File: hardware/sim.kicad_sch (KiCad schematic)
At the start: 11 parts, among them J12 PRPC006SAAN-RC, J13 G85D1160022HHR

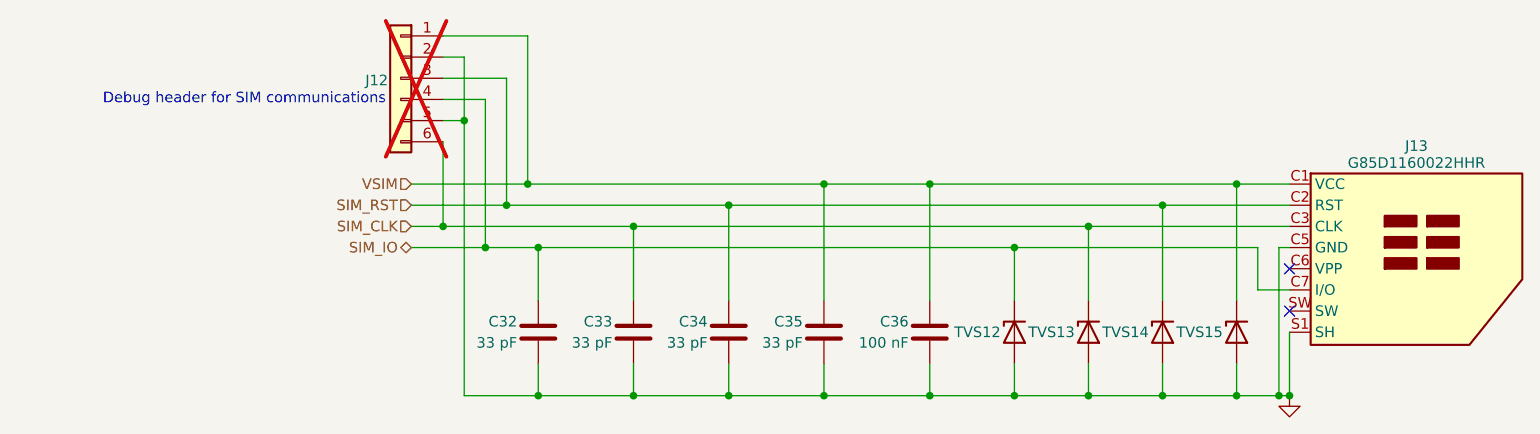
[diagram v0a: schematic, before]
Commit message: HW: Add battery protection
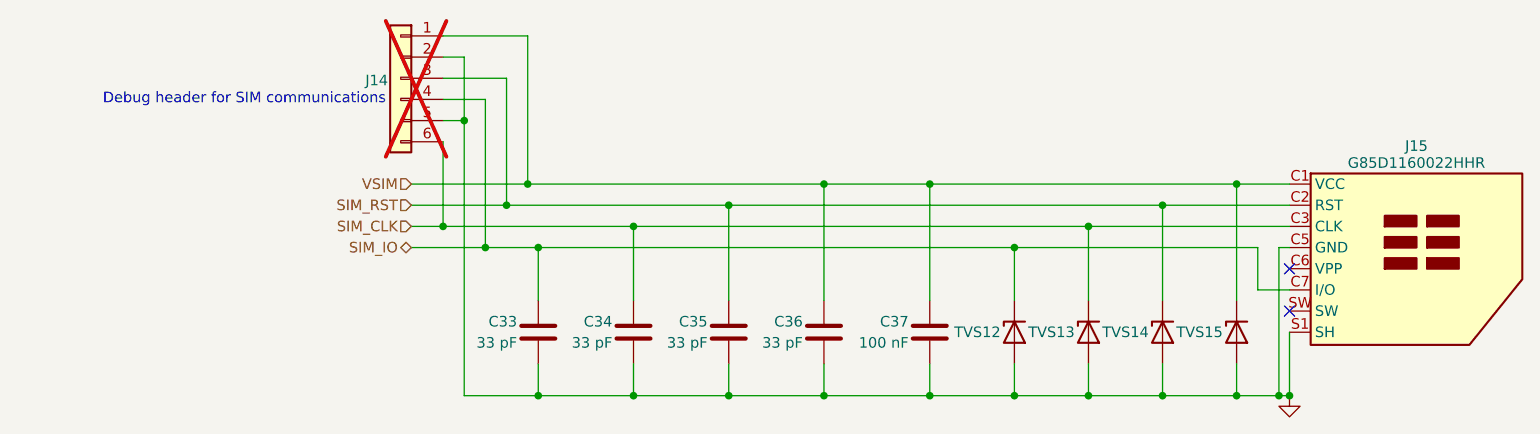
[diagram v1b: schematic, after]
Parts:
- renumbered C32 to C33, C33 to C34, C34 to C35, C35 to C36, C36 to C37, J12 to J14, J13 to J15
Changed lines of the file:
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@@
 		(on_board yes)
 		(dnp no)
-		(property "Reference" "C36"
+		(property "Reference" "C37"
 			(at 143.51 135.89 0)
 			(effects
@@
 			(project "iida_devkit"
 				(path "/b12a6e25-97fb-4aba-bc96-af8db389bb9a/33580d9f-a609-4568-baaf-9a29cf2dabcd"
-					(reference "C36")
+					(reference "C37")
 					(unit 1)
 				)
@@
 		(on_board yes)
 		(dnp yes)
-		(property "Reference" "J12"
+		(property "Reference" "J14"
 			(at 81.026 106.934 0)
 			(effects
@@
 			(project "iida_devkit"
 				(path "/b12a6e25-97fb-4aba-bc96-af8db389bb9a/33580d9f-a609-4568-baaf-9a29cf2dabcd"
-					(reference "J12")
+					(reference "J14")
 					(unit 1)
 				)
@@
 		(on_board yes)
 		(dnp no)
-		(property "Reference" "C33"
+		(property "Reference" "C34"
 			(at 107.95 135.89 0)
 			(effects
@@
 			(project "iida_devkit"
 				(path "/b12a6e25-97fb-4aba-bc96-af8db389bb9a/33580d9f-a609-4568-baaf-9a29cf2dabcd"
-					(reference "C33")
+					(reference "C34")
 					(unit 1)
 				)
@@
 		(on_board yes)
 		(dnp no)
-		(property "Reference" "C32"
+		(property "Reference" "C33"
 			(at 96.52 135.89 0)
 			(effects
@@
 			(project "iida_devkit"
 				(path "/b12a6e25-97fb-4aba-bc96-af8db389bb9a/33580d9f-a609-4568-baaf-9a29cf2dabcd"
-					(reference "C32")
+					(reference "C33")
 					(unit 1)
 				)
@@
 		(on_board yes)
 		(dnp no)
-		(property "Reference" "C34"
+		(property "Reference" "C35"
 			(at 119.38 135.89 0)
 			(effects
@@
 			(project "iida_devkit"
 				(path "/b12a6e25-97fb-4aba-bc96-af8db389bb9a/33580d9f-a609-4568-baaf-9a29cf2dabcd"
-					(reference "C34")
+					(reference "C35")
 					(unit 1)
 				)
@@
 		(on_board yes)
 		(dnp no)
-		(property "Reference" "J13"
+		(property "Reference" "J15"
 			(at 204.47 114.808 0)
 			(effects
@@
 			(project "iida_devkit"
 				(path "/b12a6e25-97fb-4aba-bc96-af8db389bb9a/33580d9f-a609-4568-baaf-9a29cf2dabcd"
-					(reference "J13")
+					(reference "J15")
 					(unit 1)
 				)
@@
 		(dnp no)
 		(fields_autoplaced yes)
-		(property "Reference" "#PWR056"
+		(property "Reference" "#PWR058"
 			(at 189.23 151.13 0)
 			(effects
@@
 			(project "iida_devkit"
 				(path "/b12a6e25-97fb-4aba-bc96-af8db389bb9a/33580d9f-a609-4568-baaf-9a29cf2dabcd"
-					(reference "#PWR056")
+					(reference "#PWR058")
 					(unit 1)
 				)
@@
 		(on_board yes)
 		(dnp no)
-		(property "Reference" "C35"
+		(property "Reference" "C36"
 			(at 130.81 135.89 0)
 			(effects
@@
 			(project "iida_devkit"
 				(path "/b12a6e25-97fb-4aba-bc96-af8db389bb9a/33580d9f-a609-4568-baaf-9a29cf2dabcd"
-					(reference "C35")
+					(reference "C36")
 					(unit 1)
 				)

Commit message: HW: Replace 0402 with 0603 or bigger
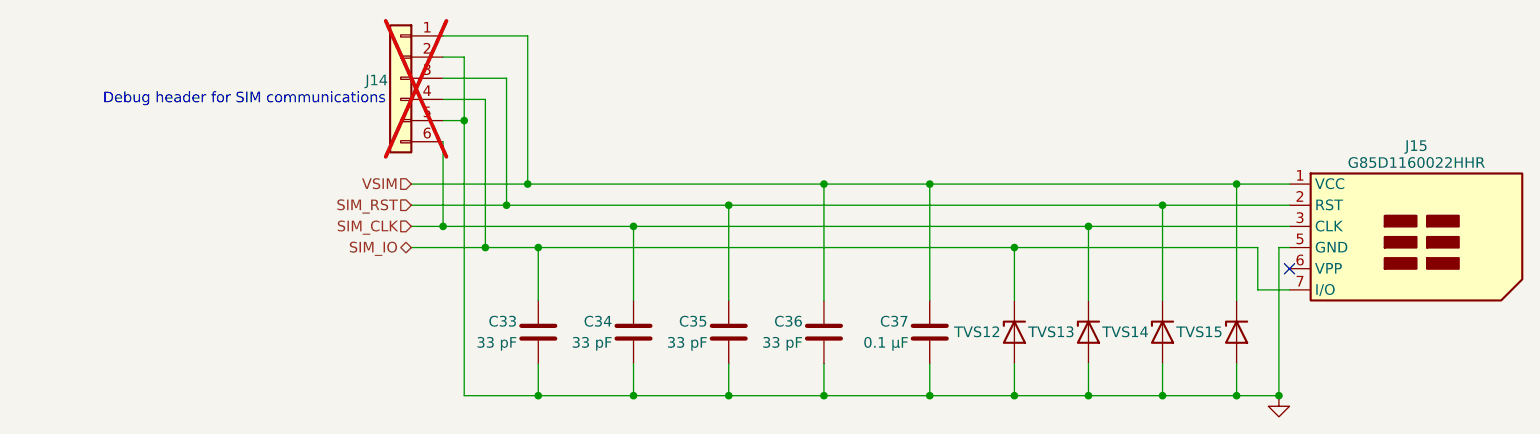
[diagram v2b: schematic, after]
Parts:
- C33, C34, C35, C36: footprint Capacitor_SMD:C_0402_1005Metric_Pad0.74x0.62mm_HandSolder -> Capacitor_SMD:C_0603_1608Metric_Pad1.08x0.95mm_HandSolder; Digi-Key Part Number 732-7472-1-ND -> 732-7749-1-ND; Manufacturer Part Number 885012005058 -> 885012006005
- C37: value 100 nF -> 0.1 µF; footprint Capacitor_SMD:C_0402_1005Metric_Pad0.74x0.62mm_HandSolder -> Capacitor_SMD:C_0603_1608Metric_Pad1.08x0.95mm_HandSolder; Digi-Key Part Number 732-7513-1-ND -> 732-7989-1-ND; Manufacturer Part Number 885012205018 -> 885012206071
- TVS12, TVS13, TVS14, TVS15: value PE1605M1Q_R1_00001 -> CPDUC5V0USP-HF; footprint Diode_SMD:D_0402_1005Metric_Pad0.77x0.64mm_HandSolder -> Diode_SMD:D_0603_1608Metric_Pad1.05x0.95mm_HandSolder; Digi-Key Part Number 3757-PE1605M1Q_R1_00001CT-ND -> 641-1765-1-ND; Manufacturer Panjit International Inc. -> Comchip Technology; Manufacturer Part Number PE1605M1Q_R1_00001 -> CPDUC5V0USP-HF
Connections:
- net GND: now also J15.5 (GND); no longer J15.C5 (GND), J15.S1 (SH), J15.S2 (SH), J15.S3 (SH)
- net SIM_CLK: now also J15.3 (CLK); no longer J15.C3 (CLK)
- net SIM_IO: now also J15.7 (I/O); no longer J15.C7 (I/O)
- net SIM_RST: now also J15.2 (RST); no longer J15.C2 (RST)
- net VSIM: now also J15.1 (VCC); no longer J15.C1 (VCC)
- no-connect marks 2 -> 1
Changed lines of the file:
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@@
 	)
 	(junction
-		(at 189.23 144.78)
-		(diameter 0)
-		(color 0 0 0 0)
-	)
-	(junction
 		(at 110.49 124.46)
 		(diameter 0)
@@
 		(at 189.23 129.54)
 	)
-	(no_connect
-		(at 189.23 134.62)
-	)
 	(wire
 		(pts
@@
 	(wire
 		(pts
-			(xy 189.23 144.78) (xy 187.96 144.78)
-		)
-		(stroke
-			(width 0)
-			(type default)
-		)
-	)
-	(wire
-		(pts
 			(xy 133.35 140.97) (xy 133.35 144.78)
 		)
@@
 	(wire
 		(pts
-			(xy 189.23 137.16) (xy 189.23 144.78)
-		)
-		(stroke
-			(width 0)
-			(type default)
-		)
-	)
-	(wire
-		(pts
 			(xy 156.21 144.78) (xy 165.1 144.78)
 		)
@@
 			)
 		)
-		(property "Value" "100 nF"
+		(property "Value" "0.1 µF"
 			(at 143.51 138.43 0)
 			(effects
@@
 			)
 		)
-		(property "Footprint" "Capacitor_SMD:C_0402_1005Metric_Pad0.74x0.62mm_HandSolder"
+		(property "Footprint" "Capacitor_SMD:C_0603_1608Metric_Pad1.08x0.95mm_HandSolder"
 			(at 145.0848 140.97 0)
 			(effects
@@
 			)
 		)
-		(property "Manufacturer Part Number" "885012205018"
+		(property "Manufacturer Part Number" "885012206071"
 			(at 146.05 137.16 0)
 			(effects
@@
 			)
 		)
-		(property "Digi-Key Part Number" "732-7513-1-ND"
+		(property "Digi-Key Part Number" "732-7989-1-ND"
 			(at 146.05 137.16 0)
 			(effects
@@
 			)
 		)
-		(property "Value" "PE1605M1Q_R1_00001"
+		(property "Value" "CPDUC5V0USP-HF"
 			(at 154.94 138.43 90)
 			(effects
@@
 			)
 		)
-		(property "Footprint" "Diode_SMD:D_0402_1005Metric_Pad0.77x0.64mm_HandSolder"
+		(property "Footprint" "Diode_SMD:D_0603_1608Metric_Pad1.05x0.95mm_HandSolder"
 			(at 165.1 137.16 0)
 			(effects
@@
 			)
 		)
-		(property "Digi-Key Part Number" "3757-PE1605M1Q_R1_00001CT-ND"
+		(property "Digi-Key Part Number" "641-1765-1-ND"
 			(at 165.1 137.16 0)
 			(effects
@@
 			)
 		)
-		(property "Manufacturer" "Panjit International Inc."
+		(property "Manufacturer" "Comchip Technology"
 			(at 165.1 137.16 0)
 			(effects
@@
 			)
 		)
-		(property "Manufacturer Part Number" "PE1605M1Q_R1_00001"
+		(property "Manufacturer Part Number" "CPDUC5V0USP-HF"
 			(at 165.1 137.16 0)
 			(effects
@@
 			)
 		)
-		(property "Footprint" "Capacitor_SMD:C_0402_1005Metric_Pad0.74x0.62mm_HandSolder"
+		(property "Footprint" "Capacitor_SMD:C_0603_1608Metric_Pad1.08x0.95mm_HandSolder"
 			(at 111.4552 140.97 0)
 			(effects
@@
 			)
 		)
-		(property "Digi-Key Part Number" "732-7472-1-ND"
+		(property "Digi-Key Part Number" "732-7749-1-ND"
 			(at 110.49 137.16 0)
 			(effects
@@
 			)
 		)
-		(property "Manufacturer Part Number" "885012005058"
+		(property "Manufacturer Part Number" "885012006005"
 			(at 110.49 137.16 0)
 			(effects
@@
 			)
 		)
-		(property "Footprint" "Capacitor_SMD:C_0402_1005Metric_Pad0.74x0.62mm_HandSolder"
+		(property "Footprint" "Capacitor_SMD:C_0603_1608Metric_Pad1.08x0.95mm_HandSolder"
 			(at 100.0252 140.97 0)
 			(effects
@@
 			)
 		)
-		(property "Digi-Key Part Number" "732-7472-1-ND"
+		(property "Digi-Key Part Number" "732-7749-1-ND"
 			(at 99.06 137.16 0)
 			(effects
@@
 			)
 		)
-		(property "Manufacturer Part Number" "885012005058"
+		(property "Manufacturer Part Number" "885012006005"
 			(at 99.06 137.16 0)
 			(effects
@@
 			)
 		)
-		(property "Value" "PE1605M1Q_R1_00001"
+		(property "Value" "CPDUC5V0USP-HF"
 			(at 172.72 138.43 90)
 			(effects
@@
 			)
 		)
-		(property "Footprint" "Diode_SMD:D_0402_1005Metric_Pad0.77x0.64mm_HandSolder"
+		(property "Footprint" "Diode_SMD:D_0603_1608Metric_Pad1.05x0.95mm_HandSolder"
 			(at 182.88 137.16 0)
 			(effects
@@
 			)
 		)
-		(property "Digi-Key Part Number" "3757-PE1605M1Q_R1_00001CT-ND"
+		(property "Digi-Key Part Number" "641-1765-1-ND"
 			(at 182.88 137.16 0)
 			(effects
@@
 			)
 		)
-		(property "Manufacturer" "Panjit International Inc."
+		(property "Manufacturer" "Comchip Technology"
 			(at 182.88 137.16 0)
 			(effects
@@
 			)
 		)
-		(property "Manufacturer Part Number" "PE1605M1Q_R1_00001"
+		(property "Manufacturer Part Number" "CPDUC5V0USP-HF"
 			(at 182.88 137.16 0)
 			(effects
@@
 			)
 		)
-		(property "Value" "PE1605M1Q_R1_00001"
+		(property "Value" "CPDUC5V0USP-HF"
 			(at 146.05 138.43 90)
 			(effects
@@
 			)
 		)
-		(property "Footprint" "Diode_SMD:D_0402_1005Metric_Pad0.77x0.64mm_HandSolder"
+		(property "Footprint" "Diode_SMD:D_0603_1608Metric_Pad1.05x0.95mm_HandSolder"
 			(at 156.21 137.16 0)
 			(effects
@@
 			)
 		)
-		(property "Digi-Key Part Number" "3757-PE1605M1Q_R1_00001CT-ND"
+		(property "Digi-Key Part Number" "641-1765-1-ND"
 			(at 156.21 137.16 0)
 			(effects
@@
 			)
 		)
-		(property "Manufacturer" "Panjit International Inc."
+		(property "Manufacturer" "Comchip Technology"
 			(at 156.21 137.16 0)
 			(effects
@@
 			)
 		)
-		(property "Manufacturer Part Number" "PE1605M1Q_R1_00001"
+		(property "Manufacturer Part Number" "CPDUC5V0USP-HF"
 			(at 156.21 137.16 0)
 			(effects
@@
 			)
 		)
-		(property "Footprint" "Capacitor_SMD:C_0402_1005Metric_Pad0.74x0.62mm_HandSolder"
+		(property "Footprint" "Capacitor_SMD:C_0603_1608Metric_Pad1.08x0.95mm_HandSolder"
 			(at 122.8852 140.97 0)
 			(effects
@@
 			)
 		)
-		(property "Digi-Key Part Number" "732-7472-1-ND"
+		(property "Digi-Key Part Number" "732-7749-1-ND"
 			(at 121.92 137.16 0)
 			(effects
@@
 			)
 		)
-		(property "Manufacturer Part Number" "885012005058"
+		(property "Manufacturer Part Number" "885012006005"
 			(at 121.92 137.16 0)
 			(effects
@@
 			)
 		)
-		(pin "C1"
-		)
-		(pin "C2"
-		)
-		(pin "C3"
-		)
-		(pin "C7"
-		)
-		(pin "S1"
+		(pin "5"
 		)
-		(pin "C5"
+		(pin "7"
 		)
-		(pin "C6"
+		(pin "3"
 		)
-		(pin "S3"
+		(pin "2"
 		)
-		(pin "SW"
+		(pin "1"
 		)
-		(pin "S2"
+		(pin "6"
 		)
 		(instances
@@
 			)
 		)
-		(property "Value" "PE1605M1Q_R1_00001"
+		(property "Value" "CPDUC5V0USP-HF"
 			(at 163.83 138.43 90)
 			(effects
@@
 			)
 		)
-		(property "Footprint" "Diode_SMD:D_0402_1005Metric_Pad0.77x0.64mm_HandSolder"
+		(property "Footprint" "Diode_SMD:D_0603_1608Metric_Pad1.05x0.95mm_HandSolder"
 			(at 173.99 137.16 0)
 			(effects
@@
 			)
 		)
-		(property "Digi-Key Part Number" "3757-PE1605M1Q_R1_00001CT-ND"
+		(property "Digi-Key Part Number" "641-1765-1-ND"
 			(at 173.99 137.16 0)
 			(effects
@@
 			)
 		)
-		(property "Manufacturer" "Panjit International Inc."
+		(property "Manufacturer" "Comchip Technology"
 			(at 173.99 137.16 0)
 			(effects
@@
 			)
 		)
-		(property "Manufacturer Part Number" "PE1605M1Q_R1_00001"
+		(property "Manufacturer Part Number" "CPDUC5V0USP-HF"
 			(at 173.99 137.16 0)
 			(effects
@@
 	(symbol
 		(lib_id "power:GND")
-		(at 189.23 144.78 0)
+		(at 187.96 144.78 0)
 		(unit 1)
 		(exclude_from_sim no)
@@
 		(fields_autoplaced yes)
 		(property "Reference" "#PWR058"
-			(at 189.23 151.13 0)
+			(at 187.96 151.13 0)
 			(effects
 				(font
@@
 		)
 		(property "Value" "GND"
-			(at 189.23 149.86 0)
+			(at 187.96 149.86 0)
 			(effects
 				(font
@@
 		)
 		(property "Footprint" ""
-			(at 189.23 144.78 0)
+			(at 187.96 144.78 0)
 			(effects
 				(font
@@
 		)
 		(property "Datasheet" ""
-			(at 189.23 144.78 0)
+			(at 187.96 144.78 0)
 			(effects
 				(font
@@
 		)
 		(property "Description" "Power symbol creates a global label with name \"GND\" , ground"
-			(at 189.23 144.78 0)
+			(at 187.96 144.78 0)
 			(effects
 				(font
@@
 			)
 		)
-		(property "Footprint" "Capacitor_SMD:C_0402_1005Metric_Pad0.74x0.62mm_HandSolder"
+		(property "Footprint" "Capacitor_SMD:C_0603_1608Metric_Pad1.08x0.95mm_HandSolder"
 			(at 134.3152 140.97 0)
 			(effects
@@
 			)
 		)
-		(property "Digi-Key Part Number" "732-7472-1-ND"
+		(property "Digi-Key Part Number" "732-7749-1-ND"
 			(at 133.35 137.16 0)
 			(effects
@@
 			)
 		)
-		(property "Manufacturer Part Number" "885012005058"
+		(property "Manufacturer Part Number" "885012006005"
 			(at 133.35 137.16 0)
 			(effects
